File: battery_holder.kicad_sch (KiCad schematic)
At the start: 12 parts, among them J1 aux pwr, J2 usb, J3 TP4056, J4 aux bat, J5 Bat+, J6 Bat-

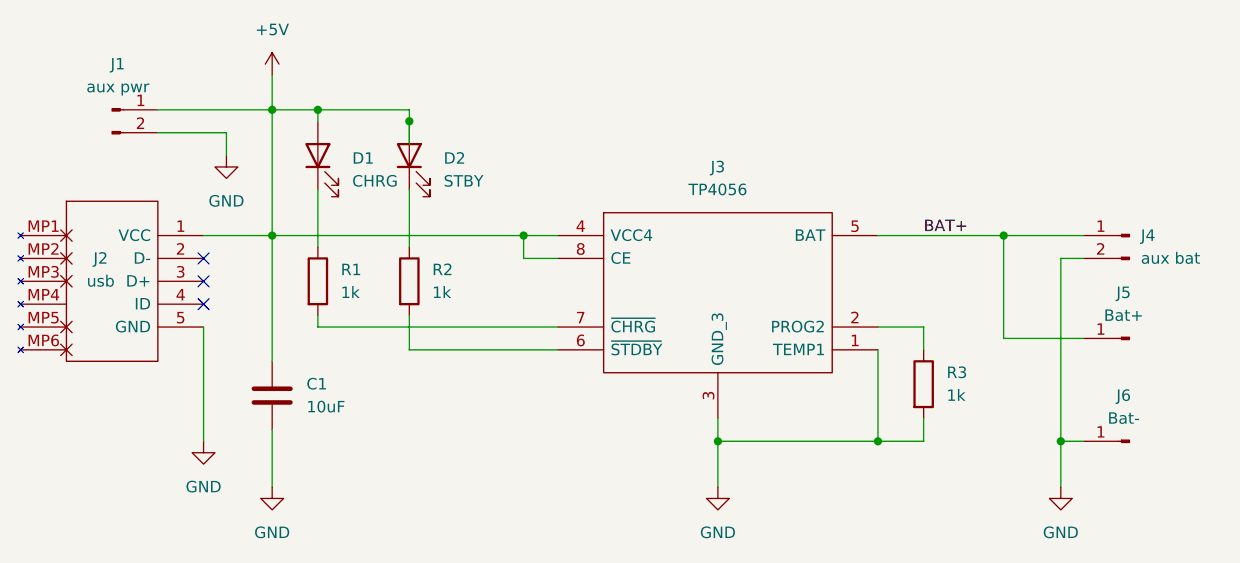
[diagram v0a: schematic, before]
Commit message: Updated template for KiCAD 7
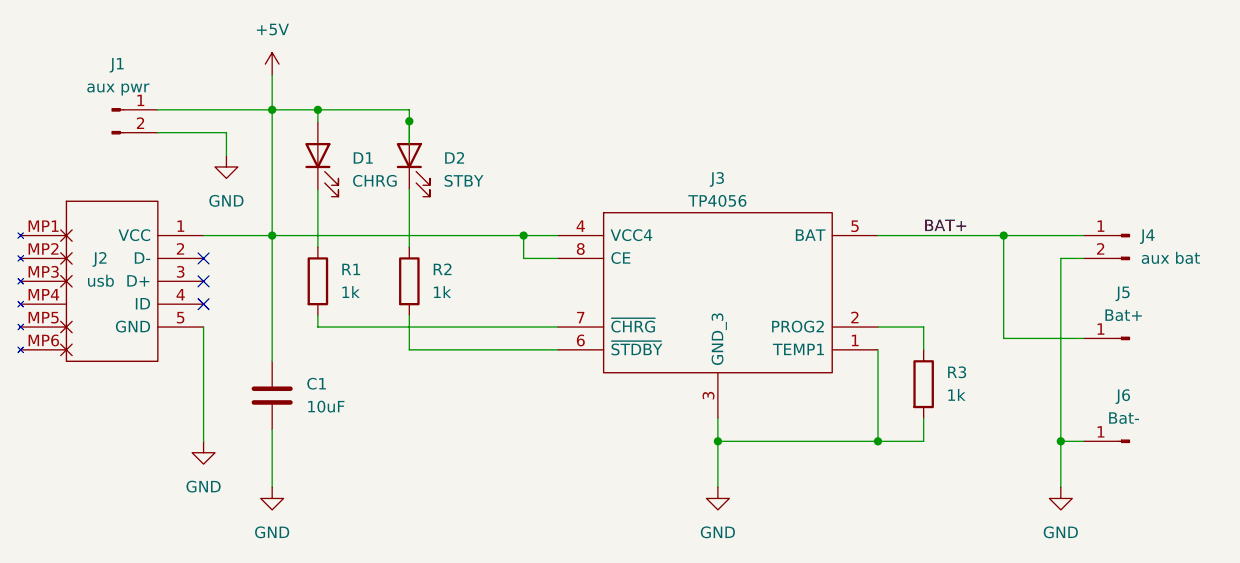
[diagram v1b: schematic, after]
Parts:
- J1, J4: symbol Connector:Conn_01x02_Male -> Chof747 Connectors:Conn_01x02_Male
- J2: symbol USB Connector 10118192-0002LF:10118192-0002LF -> Chof747 Connectors:10118192-0002LF
- J3: footprint footprints:SOP-8-Tiny Package -> SOIC127P600X175-9N; symbol TP4056:TP4056 -> Chof747 Battery Management:TP4056
- J5, J6: symbol Connector:Conn_01x01_Male -> Chof747 Connectors:Conn_01x01_Male
